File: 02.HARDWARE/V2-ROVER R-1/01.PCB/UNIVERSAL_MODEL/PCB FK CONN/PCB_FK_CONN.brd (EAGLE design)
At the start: 23.3 x 23.5 mm, 0 parts

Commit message: Pedido y actualizacion
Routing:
- net A: track 53.9 -> 56.1 mm
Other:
- board text added: ""I love it when a plan comes together""
- board text removed: "***"
- board text removed: "F Irons"
- board text removed: "K"
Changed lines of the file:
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@@
 <grid distance="0.1" unitdist="mm" unit="mm" style="lines" multiple="1" display="yes" altdistance="5" altunitdist="mil" altunit="mil"/>
 <layers>
-<layer number="1" name="Top" color="4" fill="1" visible="no" active="yes"/>
-<layer number="16" name="Bottom" color="1" fill="1" visible="yes" active="yes"/>
+<layer number="1" name="Top" color="4" fill="1" visible="yes" active="yes"/>
+<layer number="16" name="Bottom" color="1" fill="1" visible="no" active="yes"/>
 <layer number="17" name="Pads" color="2" fill="1" visible="yes" active="yes"/>
 <layer number="18" name="Vias" color="2" fill="1" visible="yes" active="yes"/>
 <layer number="19" name="Unrouted" color="6" fill="1" visible="yes" active="yes"/>
 <layer number="20" name="Dimension" color="24" fill="1" visible="yes" active="yes"/>
-<layer number="21" name="tPlace" color="7" fill="1" visible="no" active="yes"/>
-<layer number="22" name="bPlace" color="7" fill="1" visible="yes" active="yes"/>
-<layer number="23" name="tOrigins" color="15" fill="1" visible="no" active="yes"/>
-<layer number="24" name="bOrigins" color="15" fill="1" visible="yes" active="yes"/>
-<layer number="25" name="tNames" color="7" fill="1" visible="no" active="yes"/>
-<layer number="26" name="bNames" color="7" fill="1" visible="yes" active="yes"/>
+<layer number="21" name="tPlace" color="7" fill="1" visible="yes" active="yes"/>
+<layer number="22" name="bPlace" color="7" fill="1" visible="no" active="yes"/>
+<layer number="23" name="tOrigins" color="15" fill="1" visible="yes" active="yes"/>
+<layer number="24" name="bOrigins" color="15" fill="1" visible="no" active="yes"/>
+<layer number="25" name="tNames" color="7" fill="1" visible="yes" active="yes"/>
+<layer number="26" name="bNames" color="7" fill="1" visible="no" active="yes"/>
 <layer number="27" name="tValues" color="7" fill="1" visible="no" active="yes"/>
 <layer number="28" name="bValues" color="7" fill="1" visible="no" active="yes"/>
@@
 <layer number="37" name="tTest" color="7" fill="1" visible="no" active="yes"/>
 <layer number="38" name="bTest" color="7" fill="1" visible="no" active="yes"/>
-<layer number="39" name="tKeepout" color="4" fill="11" visible="no" active="yes"/>
-<layer number="40" name="bKeepout" color="1" fill="11" visible="yes" active="yes"/>
-<layer number="41" name="tRestrict" color="4" fill="10" visible="no" active="yes"/>
-<layer number="42" name="bRestrict" color="1" fill="10" visible="yes" active="yes"/>
+<layer number="39" name="tKeepout" color="4" fill="11" visible="yes" active="yes"/>
+<layer number="40" name="bKeepout" color="1" fill="11" visible="no" active="yes"/>
+<layer number="41" name="tRestrict" color="4" fill="10" visible="yes" active="yes"/>
+<layer number="42" name="bRestrict" color="1" fill="10" visible="no" active="yes"/>
 <layer number="43" name="vRestrict" color="2" fill="10" visible="no" active="yes"/>
 <layer number="44" name="Drills" color="7" fill="1" visible="no" active="yes"/>
@@
 <layer number="49" name="Reference" color="7" fill="1" visible="no" active="yes"/>
 <layer number="50" name="dxf" color="7" fill="1" visible="no" active="no"/>
-<layer number="51" name="tDocu" color="7" fill="1" visible="no" active="yes"/>
-<layer number="52" name="bDocu" color="7" fill="1" visible="yes" active="yes"/>
+<layer number="51" name="tDocu" color="7" fill="1" visible="yes" active="yes"/>
+<layer number="52" name="bDocu" color="7" fill="1" visible="no" active="yes"/>
 <layer number="53" name="tGND_GNDA" color="7" fill="9" visible="no" active="no"/>
 <layer number="54" name="bGND_GNDA" color="1" fill="9" visible="no" active="no"/>
@@
 <text x="75" y="63.5" size="1.016" layer="22" font="vector" rot="MR0">FK_CONN
 v1-Feb24</text>
-<text x="73" y="69.85" size="1.016" layer="22" font="vector" rot="MR0">F
-Irons</text>
-<text x="72.5" y="71.4" size="0.1" layer="22" font="vector" rot="MR0">***</text>
-<text x="71.9" y="71.37" size="1.016" layer="22" font="vector" rot="MR0">K</text>
+<text x="75.8" y="68.45" size="1.016" layer="22" font="vector" rot="MR0">"I love it
+when a plan
+comes
+together"</text>
 </plain>
 <attributes>
@@
 <wire x1="75.979" y1="71.274" x2="78.679" y2="71.274" width="1.016" layer="16"/>
 <wire x1="78.679" y1="71.274" x2="78.732" y2="71.327" width="1.016" layer="16"/>
-<wire x1="69.962" y1="67.842" x2="68.175" y2="69.629" width="1.016" layer="16"/>
-<wire x1="68.175" y1="69.629" x2="68.175" y2="70.96" width="1.016" layer="16"/>
-<wire x1="68.175" y1="70.96" x2="68.175" y2="72.379" width="1.016" layer="16"/>
-<wire x1="68.175" y1="72.379" x2="69.774" y2="73.978" width="1.016" layer="16"/>
+<wire x1="69.962" y1="67.842" x2="68.275" y2="69.529" width="1.016" layer="16"/>
+<wire x1="68.275" y1="70.86" x2="68.275" y2="69.529" width="1.016" layer="16"/>
+<wire x1="68.275" y1="70.86" x2="68.175" y2="70.96" width="1.016" layer="16"/>
+<wire x1="68.175" y1="70.96" x2="68.275" y2="71.06" width="1.016" layer="16"/>
+<wire x1="68.275" y1="72.479" x2="68.275" y2="71.06" width="1.016" layer="16"/>
+<wire x1="68.275" y1="72.479" x2="69.774" y2="73.978" width="1.016" layer="16"/>
 <wire x1="69.774" y1="73.978" x2="69.981" y2="74.185" width="1.016" layer="16"/>
 <wire x1="69.981" y1="74.185" x2="73.829" y2="74.185" width="1.016" layer="16"/>
 <wire x1="73.829" y1="74.185" x2="75.979" y2="72.035" width="1.016" layer="16"/>
 <wire x1="75.979" y1="72.035" x2="75.979" y2="71.274" width="1.016" layer="16"/>
-<wire x1="75.979" y1="69.53" x2="74.251" y2="67.802" width="1.016" layer="16"/>
-<wire x1="74.214" y1="67.802" x2="74.251" y2="67.802" width="1.016" layer="16"/>
-<wire x1="75.979" y1="69.53" x2="75.979" y2="71.274" width="1.016" layer="16"/>
+<wire x1="74.214" y1="67.802" x2="74.214" y2="69.565" width="1.016" layer="16"/>
+<wire x1="74.379" y1="69.73" x2="74.214" y2="69.565" width="1.016" layer="16"/>
+<wire x1="74.435" y1="69.73" x2="75.979" y2="71.274" width="1.016" layer="16"/>
+<wire x1="74.435" y1="69.73" x2="74.379" y2="69.73" width="1.016" layer="16"/>
 <wire x1="73.829" y1="74.185" x2="75.51" y2="75.866" width="1.016" layer="1"/>
 <wire x1="75.51" y1="75.866" x2="75.51" y2="75.89" width="1.016" layer="1"/>
@@
 <via x="72.101" y="61.45" extent="1-16" drill="0.35"/>
 <via x="63.294" y="67.055" extent="1-16" drill="0.35"/>
-<wire x1="63.294" y1="67.055" x2="65.086" y2="67.055" width="1.016" layer="16"/>
-<wire x1="63.796" y1="75.91" x2="63.796" y2="75.513" width="1.016" layer="16"/>
-<wire x1="65.086" y1="74.223" x2="63.796" y2="75.513" width="1.016" layer="16"/>
-<wire x1="65.086" y1="74.223" x2="65.086" y2="67.055" width="1.016" layer="16"/>
-<wire x1="72.006" y1="80.575" x2="72.006" y2="79.96" width="1.016" layer="16"/>
-<wire x1="72.006" y1="79.96" x2="67.956" y2="75.91" width="1.016" layer="16"/>
-<wire x1="63.796" y1="75.91" x2="67.956" y2="75.91" width="1.016" layer="16"/>
+<wire x1="65.786" y1="66.955" x2="63.394" y2="66.955" width="1.016" layer="16"/>
+<wire x1="63.294" y1="67.055" x2="63.394" y2="66.955" width="1.016" layer="16"/>
+<wire x1="63.796" y1="75.91" x2="65.786" y2="75.91" width="1.016" layer="16"/>
+<wire x1="65.786" y1="75.91" x2="65.786" y2="66.955" width="1.016" layer="16"/>
+<wire x1="72.006" y1="80.575" x2="72.006" y2="79.36" width="1.016" layer="16"/>
+<wire x1="72.006" y1="79.36" x2="68.556" y2="75.91" width="1.016" layer="16"/>
+<wire x1="63.796" y1="75.91" x2="68.556" y2="75.91" width="1.016" layer="16"/>
 <wire x1="73.86" y1="77.347" x2="79.091" y2="77.347" width="1.016" layer="16"/>
 <wire x1="72.006" y1="80.575" x2="72.006" y2="79.201" width="1.016" layer="16"/>
 <wire x1="73.86" y1="77.347" x2="72.006" y2="79.201" width="1.016" layer="16"/>
 <wire x1="80.13" y1="65.973" x2="78.748" y2="64.591" width="1.016" layer="16"/>
-<wire x1="78.748" y1="64.591" x2="73.18" y2="64.591" width="1.016" layer="16"/>
-<wire x1="73.18" y1="64.591" x2="72.101" y2="63.512" width="1.016" layer="16"/>
-<wire x1="72.101" y1="63.512" x2="72.101" y2="61.45" width="1.016" layer="16"/>
+<wire x1="78.748" y1="64.591" x2="73.88" y2="64.591" width="1.016" layer="16"/>
+<wire x1="73.88" y1="64.591" x2="72.101" y2="62.812" width="1.016" layer="16"/>
+<wire x1="72.101" y1="62.812" x2="72.101" y2="61.45" width="1.016" layer="16"/>
 <wire x1="72.101" y1="61.45" x2="72.101" y2="62.749" width="1.016" layer="16"/>
 <wire x1="72.101" y1="62.749" x2="70.09" y2="64.76" width="1.016" layer="16"/>
-<wire x1="70.09" y1="64.76" x2="67.413" y2="64.76" width="1.016" layer="16"/>
-<wire x1="67.413" y1="64.76" x2="65.118" y2="67.055" width="1.016" layer="16"/>
-<wire x1="65.118" y1="67.055" x2="63.294" y2="67.055" width="1.016" layer="16"/>
+<wire x1="70.09" y1="64.76" x2="67.813" y2="64.76" width="1.016" layer="16"/>
+<wire x1="67.813" y1="64.76" x2="65.518" y2="67.055" width="1.016" layer="16"/>
+<wire x1="65.518" y1="67.055" x2="63.294" y2="67.055" width="1.016" layer="16"/>
 </signal>
 </signals>

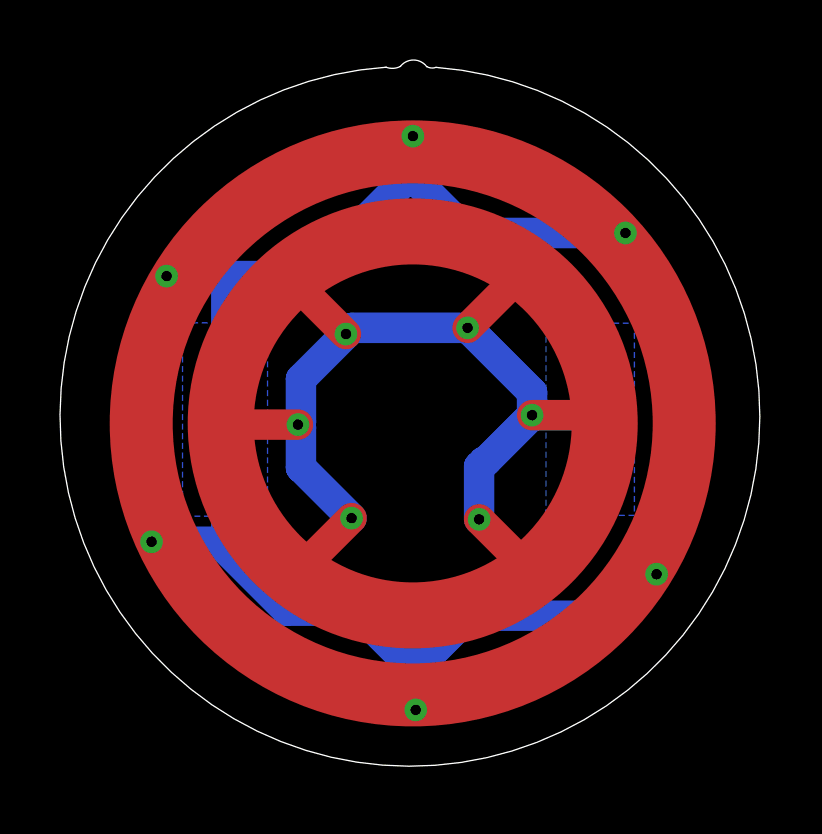
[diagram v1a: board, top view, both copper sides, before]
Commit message: PCB FK DIANA v2. se estrecha un poco el pcb pasra entrar mejor en la mecanica
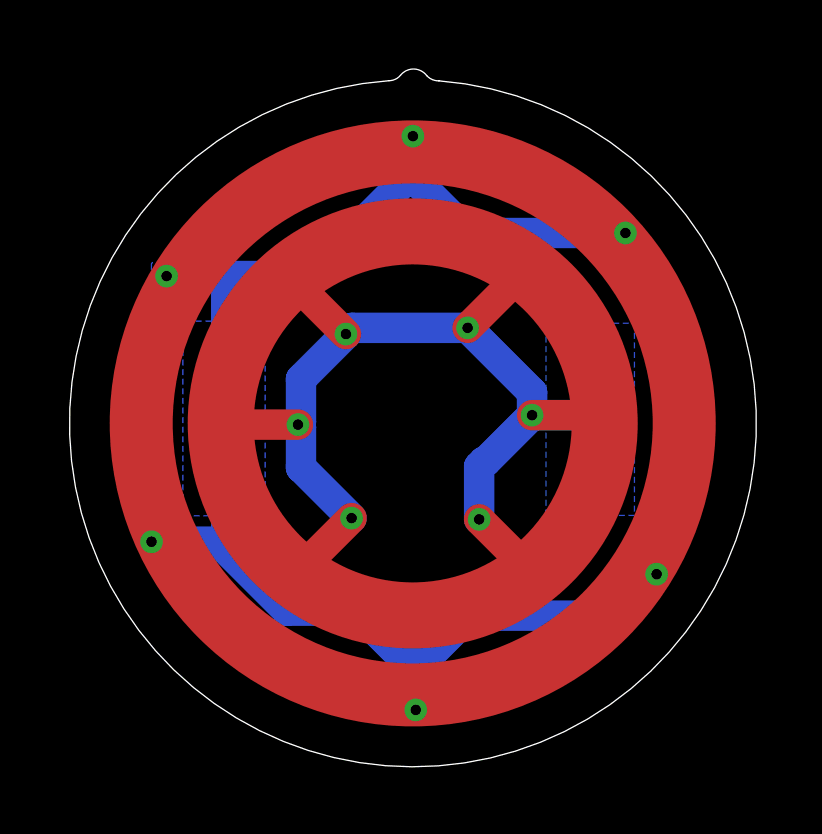
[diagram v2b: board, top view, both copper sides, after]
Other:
- board size 23.3 x 23.5 mm -> 22.9 x 23.3 mm
- board text added: "FK_CONN v2-Jul'24"
- board text removed: "FK_CONN v1-Feb24"
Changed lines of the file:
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@@
 <setting verticaltext="up"/>
 </settings>
-<grid distance="0.1" unitdist="mm" unit="mm" style="lines" multiple="1" display="yes" altdistance="5" altunitdist="mil" altunit="mil"/>
+<grid distance="0.01" unitdist="mm" unit="mm" style="lines" multiple="1" display="yes" altdistance="5" altunitdist="mil" altunit="mil"/>
 <layers>
-<layer number="1" name="Top" color="4" fill="1" visible="yes" active="yes"/>
-<layer number="16" name="Bottom" color="1" fill="1" visible="no" active="yes"/>
+<layer number="1" name="Top" color="4" fill="1" visible="no" active="yes"/>
+<layer number="16" name="Bottom" color="1" fill="1" visible="yes" active="yes"/>
 <layer number="17" name="Pads" color="2" fill="1" visible="yes" active="yes"/>
 <layer number="18" name="Vias" color="2" fill="1" visible="yes" active="yes"/>
 <layer number="19" name="Unrouted" color="6" fill="1" visible="yes" active="yes"/>
 <layer number="20" name="Dimension" color="24" fill="1" visible="yes" active="yes"/>
-<layer number="21" name="tPlace" color="7" fill="1" visible="yes" active="yes"/>
-<layer number="22" name="bPlace" color="7" fill="1" visible="no" active="yes"/>
-<layer number="23" name="tOrigins" color="15" fill="1" visible="yes" active="yes"/>
-<layer number="24" name="bOrigins" color="15" fill="1" visible="no" active="yes"/>
-<layer number="25" name="tNames" color="7" fill="1" visible="yes" active="yes"/>
-<layer number="26" name="bNames" color="7" fill="1" visible="no" active="yes"/>
+<layer number="21" name="tPlace" color="7" fill="1" visible="no" active="yes"/>
+<layer number="22" name="bPlace" color="7" fill="1" visible="yes" active="yes"/>
+<layer number="23" name="tOrigins" color="15" fill="1" visible="no" active="yes"/>
+<layer number="24" name="bOrigins" color="15" fill="1" visible="yes" active="yes"/>
+<layer number="25" name="tNames" color="7" fill="1" visible="no" active="yes"/>
+<layer number="26" name="bNames" color="7" fill="1" visible="yes" active="yes"/>
 <layer number="27" name="tValues" color="7" fill="1" visible="no" active="yes"/>
 <layer number="28" name="bValues" color="7" fill="1" visible="no" active="yes"/>
@@
 <layer number="37" name="tTest" color="7" fill="1" visible="no" active="yes"/>
 <layer number="38" name="bTest" color="7" fill="1" visible="no" active="yes"/>
-<layer number="39" name="tKeepout" color="4" fill="11" visible="yes" active="yes"/>
-<layer number="40" name="bKeepout" color="1" fill="11" visible="no" active="yes"/>
-<layer number="41" name="tRestrict" color="4" fill="10" visible="yes" active="yes"/>
-<layer number="42" name="bRestrict" color="1" fill="10" visible="no" active="yes"/>
+<layer number="39" name="tKeepout" color="4" fill="11" visible="no" active="yes"/>
+<layer number="40" name="bKeepout" color="1" fill="11" visible="yes" active="yes"/>
+<layer number="41" name="tRestrict" color="4" fill="10" visible="no" active="yes"/>
+<layer number="42" name="bRestrict" color="1" fill="10" visible="yes" active="yes"/>
 <layer number="43" name="vRestrict" color="2" fill="10" visible="no" active="yes"/>
 <layer number="44" name="Drills" color="7" fill="1" visible="no" active="yes"/>
@@
 <layer number="49" name="Reference" color="7" fill="1" visible="no" active="yes"/>
 <layer number="50" name="dxf" color="7" fill="1" visible="no" active="no"/>
-<layer number="51" name="tDocu" color="7" fill="1" visible="yes" active="yes"/>
-<layer number="52" name="bDocu" color="7" fill="1" visible="no" active="yes"/>
+<layer number="51" name="tDocu" color="7" fill="1" visible="no" active="yes"/>
+<layer number="52" name="bDocu" color="7" fill="1" visible="yes" active="yes"/>
 <layer number="53" name="tGND_GNDA" color="7" fill="9" visible="no" active="no"/>
 <layer number="54" name="bGND_GNDA" color="1" fill="9" visible="no" active="no"/>
@@
 <board>
 <plain>
-<wire x1="72.466109375" y1="82.89346875" x2="72.773509375" y2="82.86830625" width="0.001" layer="20" curve="48.464246"/>
-<wire x1="71.110490625" y1="82.873309375" x2="71.589890625" y2="82.899471875" width="0.001" layer="20" curve="48.46403"/>
-<wire x1="72.466109375" y1="82.89346875" x2="71.589890625" y2="82.899471875" width="0.001" layer="20" curve="105.105949"/>
+<wire x1="72.466109375" y1="82.59346875" x2="72.873509375" y2="82.41830625" width="0.001" layer="20" curve="48.464246"/>
+<wire x1="71.210490625" y1="82.423309375" x2="71.589890625" y2="82.599471875" width="0.001" layer="20" curve="48.46403"/>
+<wire x1="72.466109375" y1="82.59346875" x2="71.589890625" y2="82.599471875" width="0.001" layer="20" curve="105.105949"/>
 <circle x="72" y="71" radius="6.4" width="2.2" layer="29"/>
-<wire x1="71.110490625" y1="82.873309375" x2="72.773509375" y2="82.86830625" width="0.001" layer="20" curve="351.823836"/>
+<wire x1="71.210490625" y1="82.423309375" x2="72.873509375" y2="82.41830625" width="0.001" layer="20" curve="351.67"/>
 <circle x="72" y="71" radius="9.05" width="2.1" layer="29"/>
 <circle x="72" y="71" radius="10.1" width="0.001" layer="48"/>
@@
 <text x="67.7" y="74.9" size="1.778" layer="22" font="vector" rot="MR0">EXT</text>
 <text x="79.6" y="74.8" size="1.778" layer="22" font="vector" rot="MR0">INT</text>
-<text x="75" y="63.5" size="1.016" layer="22" font="vector" rot="MR0">FK_CONN
-v1-Feb24</text>
+<text x="75" y="63.46" size="1.016" layer="22" font="vector" rot="MR0">FK_CONN
+v2-Jul'24</text>
 <text x="75.8" y="68.45" size="1.016" layer="22" font="vector" rot="MR0">"I love it
 when a plan
@@
 </signal>
 <signal name="A">
-<polygon width="0.1524" layer="16">
-<vertex x="64.327" y="67.911"/>
-<vertex x="64.327" y="74.349"/>
-<vertex x="67.161" y="74.349"/>
-<vertex x="67.161" y="67.911"/>
-</polygon>
 <via x="63.796" y="75.91" extent="1-16" drill="0.35"/>
 <via x="72.006" y="80.575" extent="1-16" drill="0.35"/>
@@
 <wire x1="67.813" y1="64.76" x2="65.518" y2="67.055" width="1.016" layer="16"/>
 <wire x1="65.518" y1="67.055" x2="63.294" y2="67.055" width="1.016" layer="16"/>
+<polygon width="0.1524" layer="16">
+<vertex x="63.29" y="76.32"/>
+<vertex x="63.29" y="75.48"/>
+<vertex x="63.4" y="75.37"/>
+<vertex x="65.33" y="75.37"/>
+<vertex x="65.35" y="75.35"/>
+<vertex x="65.35" y="74.47"/>
+<vertex x="65.29" y="74.41"/>
+<vertex x="64.34" y="74.41"/>
+<vertex x="64.34" y="67.96"/>
+<vertex x="64.38" y="67.92"/>
+<vertex x="67.08" y="67.92"/>
+<vertex x="67.08" y="74.49"/>
+<vertex x="66.34" y="74.49"/>
+<vertex x="66.24" y="74.59"/>
+<vertex x="66.24" y="76.34"/>
+<vertex x="66.22" y="76.36"/>
+<vertex x="63.31" y="76.36"/>
+</polygon>
 </signal>
 </signals>
